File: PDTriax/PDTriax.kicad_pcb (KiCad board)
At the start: 2 copper layers, 25.4 x 25.4 mm, 2 parts, among them J1 TO-5 Photodiode Socket, J2 CBJ70

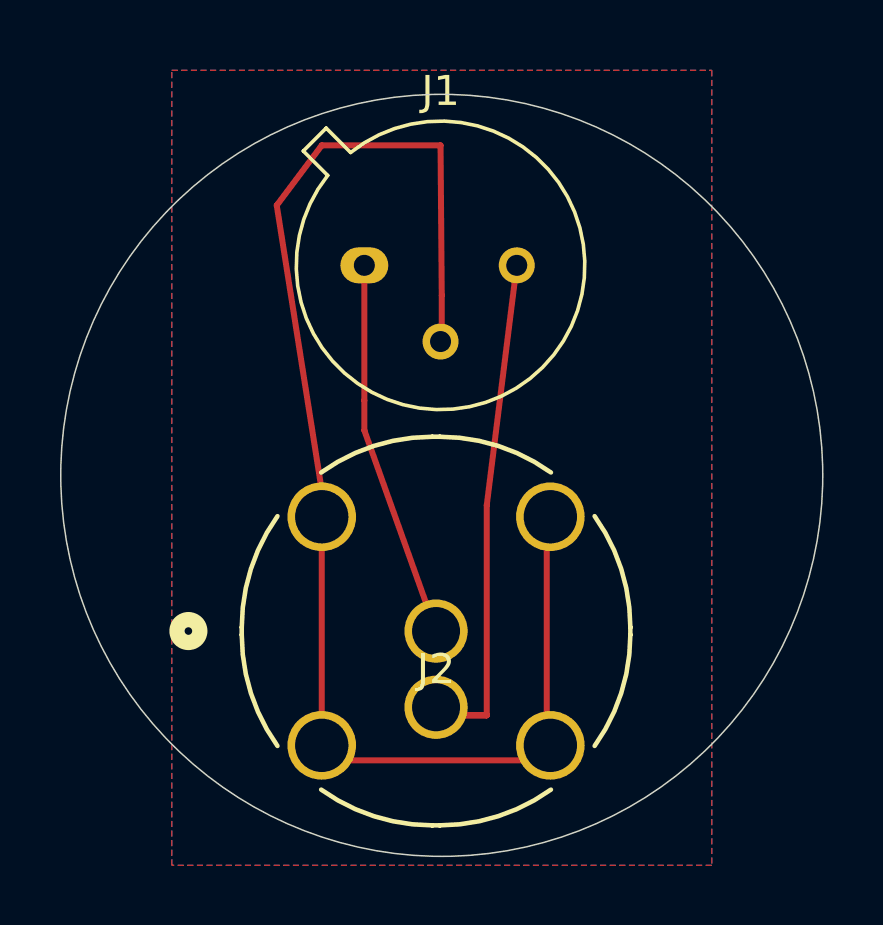
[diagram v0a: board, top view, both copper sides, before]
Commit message: Changed Wires
I previously made wires with lines, which was incorrect, so changed them to tracks.
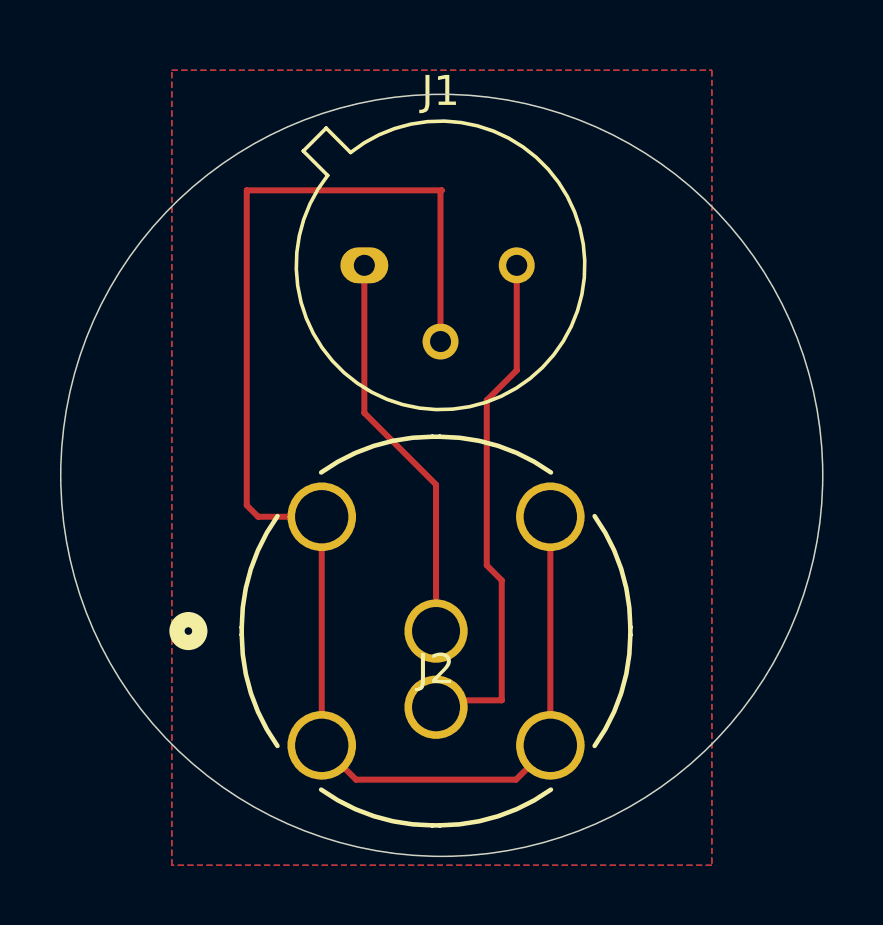
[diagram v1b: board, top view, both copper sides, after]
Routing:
- net GND: track 0.00 -> 48.5 mm
- net /OUT: track 0.00 -> 17.4 mm
- net /IN: track 0.00 -> 13.2 mm
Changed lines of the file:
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@@
 		(embedded_fonts no)
-	)
-	(gr_line
-		(start 183.5 83.5)
-		(end 183.5 77)
-		(stroke
-			(width 0.2)
-			(type default)
-		)
-		(layer "F.Cu")
-		(net 3)
-	)
-	(gr_line
-		(start 174.5 66.5)
-		(end 176 76)
-		(stroke
-			(width 0.2)
-			(type default)
-		)
-		(layer "F.Cu")
-		(net 3)
-	)
-	(gr_line
-		(start 181.5 83.5)
-		(end 180 83.5)
-		(stroke
-			(width 0.2)
-			(type default)
-		)
-		(layer "F.Cu")
-		(net 1)
-	)
-	(gr_line
-		(start 181.5 76.5)
-		(end 181.5 83.5)
-		(stroke
-			(width 0.2)
-			(type default)
-		)
-		(layer "F.Cu")
-		(net 1)
-	)
-	(gr_line
-		(start 177.42 74)
-		(end 179.81 80.69)
-		(stroke
-			(width 0.2)
-			(type default)
-		)
-		(layer "F.Cu")
-		(net 2)
-	)
-	(gr_line
-		(start 180 69.5)
-		(end 179.96 64.5)
-		(stroke
-			(width 0.2)
-			(type default)
-		)
-		(layer "F.Cu")
-		(net 3)
-	)
-	(gr_line
-		(start 177.42 68.5)
-		(end 177.42 73)
-		(stroke
-			(width 0.2)
-			(type default)
-		)
-		(layer "F.Cu")
-		(net 2)
-	)
-	(gr_line
-		(start 182.5 68.5)
-		(end 181.5 76.5)
-		(stroke
-			(width 0.2)
-			(type default)
-		)
-		(layer "F.Cu")
-		(net 1)
-	)
-	(gr_line
-		(start 174.5 66.5)
-		(end 176 64.5)
-		(stroke
-			(width 0.2)
-			(type default)
-		)
-		(layer "F.Cu")
-		(net 3)
-	)
-	(gr_line
-		(start 179.96 64.5)
-		(end 176 64.5)
-		(stroke
-			(width 0.2)
-			(type default)
-		)
-		(layer "F.Cu")
-		(net 3)
-	)
-	(gr_line
-		(start 176 76)
-		(end 176 85)
-		(stroke
-			(width 0.2)
-			(type default)
-		)
-		(layer "F.Cu")
-		(net 3)
-	)
-	(gr_line
-		(start 180 69.5)
-		(end 180 71)
-		(stroke
-			(width 0.2)
-			(type default)
-		)
-		(layer "F.Cu")
-		(net 3)
-	)
-	(gr_line
-		(start 176 85)
-		(end 183.5 85)
-		(stroke
-			(width 0.2)
-			(type default)
-		)
-		(layer "F.Cu")
-		(net 3)
-	)
-	(gr_line
-		(start 180.5 83.5)
-		(end 181.5 83.5)
-		(stroke
-			(width 0.2)
-			(type default)
-		)
-		(layer "F.Cu")
-		(net 1)
-	)
-	(gr_line
-		(start 177.42 73)
-		(end 177.42 74)
-		(stroke
-			(width 0.2)
-			(type default)
-		)
-		(layer "F.Cu")
-		(net 2)
 	)
 	(gr_circle
@@
 		(layer "Edge.Cuts")
 	)
+	(segment
+		(start 182 79)
+		(end 182 83)
+		(width 0.2)
+		(layer "F.Cu")
+		(net 1)
+	)
+	(segment
+		(start 182.5 68.5)
+		(end 182.5 72)
+		(width 0.2)
+		(layer "F.Cu")
+		(net 1)
+	)
+	(segment
+		(start 181.5 78.5)
+		(end 182 79)
+		(width 0.2)
+		(layer "F.Cu")
+		(net 1)
+	)
+	(segment
+		(start 182 83)
+		(end 180.04 83)
+		(width 0.2)
+		(layer "F.Cu")
+		(net 1)
+	)
+	(segment
+		(start 181.5 73)
+		(end 181.5 78.5)
+		(width 0.2)
+		(layer "F.Cu")
+		(net 1)
+	)
+	(segment
+		(start 182.5 72)
+		(end 181.5 73)
+		(width 0.2)
+		(layer "F.Cu")
+		(net 1)
+	)
+	(segment
+		(start 180.04 83)
+		(end 179.81 83.23)
+		(width 0.2)
+		(layer "F.Cu")
+		(net 1)
+	)
+	(segment
+		(start 177.42 73.42)
+		(end 179.81 75.81)
+		(width 0.2)
+		(layer "F.Cu")
+		(net 2)
+	)
+	(segment
+		(start 179.81 75.81)
+		(end 179.81 80.69)
+		(width 0.2)
+		(layer "F.Cu")
+		(net 2)
+	)
+	(segment
+		(start 177.42 68.5)
+		(end 177.42 73.42)
+		(width 0.2)
+		(layer "F.Cu")
+		(net 2)
+	)
+	(segment
+		(start 179.96 71.04)
+		(end 179.96 66.04)
+		(width 0.2)
+		(layer "F.Cu")
+		(net 3)
+	)
+	(segment
+		(start 179.96 66.04)
+		(end 180 66)
+		(width 0.2)
+		(layer "F.Cu")
+		(net 3)
+	)
+	(segment
+		(start 182.477 85.643)
+		(end 183.62 84.5)
+		(width 0.2)
+		(layer "F.Cu")
+		(net 3)
+	)
+	(segment
+		(start 176 84.5)
+		(end 177.143 85.643)
+		(width 0.2)
+		(layer "F.Cu")
+		(net 3)
+	)
+	(segment
+		(start 173.5 76.5)
+		(end 173.88 76.88)
+		(width 0.2)
+		(layer "F.Cu")
+		(net 3)
+	)
+	(segment
+		(start 177.143 85.643)
+		(end 182.477 85.643)
+		(width 0.2)
+		(layer "F.Cu")
+		(net 3)
+	)
+	(segment
+		(start 176 76.88)
+		(end 176 84.5)
+		(width 0.2)
+		(layer "F.Cu")
+		(net 3)
+	)
+	(segment
+		(start 180 66)
+		(end 173.5 66)
+		(width 0.2)
+		(layer "F.Cu")
+		(net 3)
+	)
+	(segment
+		(start 173.5 66)
+		(end 173.5 76.5)
+		(width 0.2)
+		(layer "F.Cu")
+		(net 3)
+	)
+	(segment
+		(start 183.62 84.5)
+		(end 183.62 76.88)
+		(width 0.2)
+		(layer "F.Cu")
+		(net 3)
+	)
+	(segment
+		(start 173.88 76.88)
+		(end 176 76.88)
+		(width 0.2)
+		(layer "F.Cu")
+		(net 3)
+	)
 	(zone
 		(net 3)
@@
 		(connect_pads
 			(clearance 0.5)
+		)
+		(min_thickness 0.25)
+		(filled_areas_thickness no)
+		(fill yes
+			(thermal_gap 0.5)
+			(thermal_bridge_width 0.5)
+		)
+		(polygon
+			(pts
+				(xy 171 62) (xy 189 62) (xy 189 88.5) (xy 171 88.5)
+			)
+		)
+	)
+	(zone
+		(net 3)
+		(net_name "GND")
+		(layer "F.Cu")
+		(hatch edge 0.5)
+		(priority 1)
+		(connect_pads
+			(clearance 0.5)
